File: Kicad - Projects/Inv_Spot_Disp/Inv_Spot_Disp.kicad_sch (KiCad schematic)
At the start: 38 parts, among them J1 PWM_Out, J2 Power_Supply, J3 Trigger, J4 Prog, SW1 1, SW2 2, SW3 3, SW4 4, SW5 SW_Push, U1 STM32F030F4Px, U2 NHD-0420H1Z, U3 AMS1117-3.3, U4 LKS561, U5 L7805, U6 LTV-817S

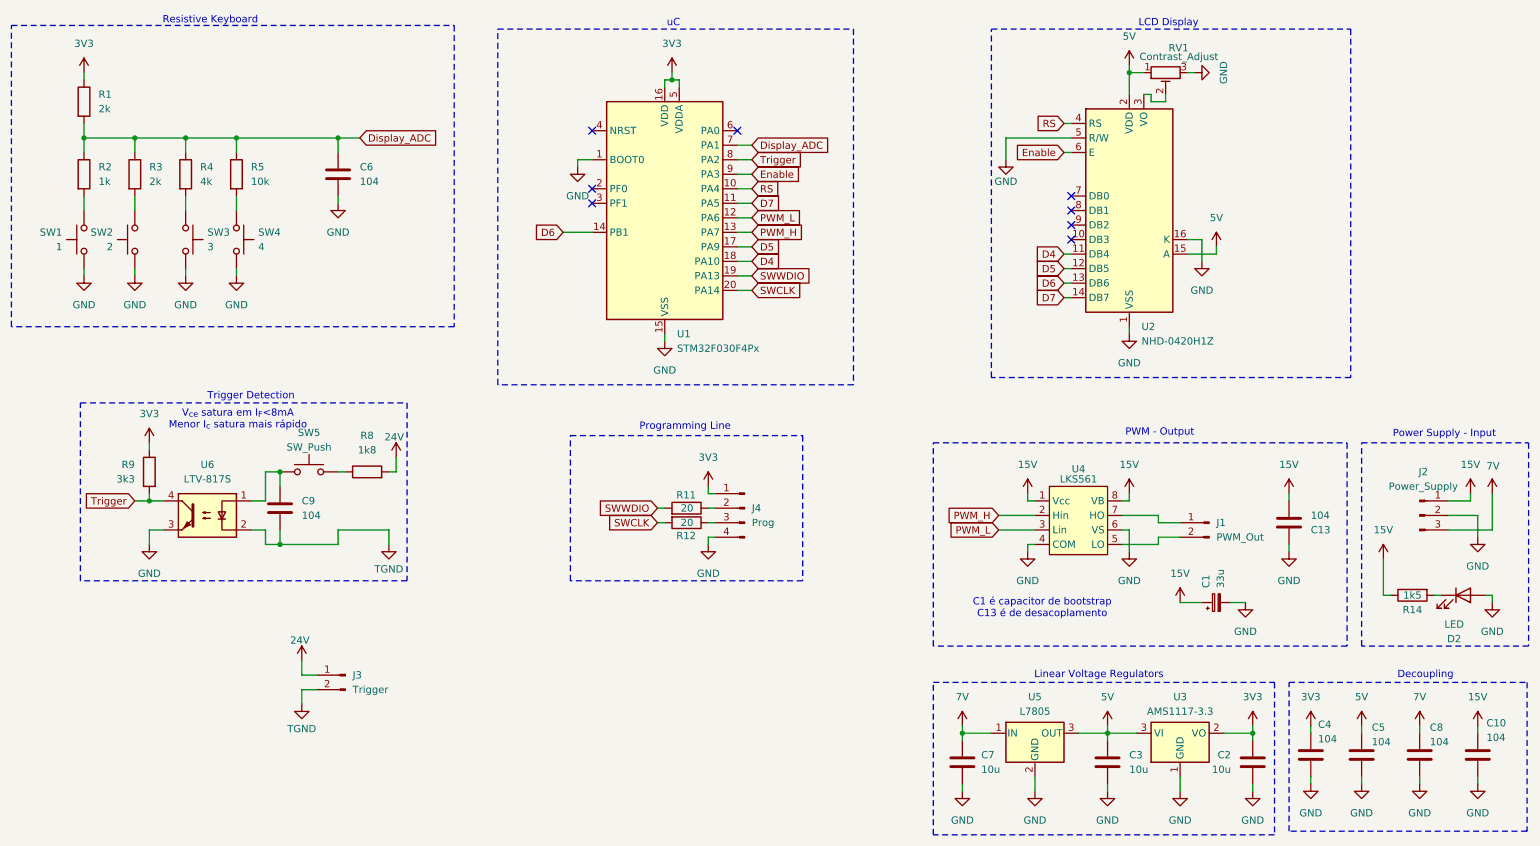
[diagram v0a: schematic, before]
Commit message: Adicionada Fuaração
Adicionada furação de montagem na placa de display, 4 furos M3 nos cantos da placa
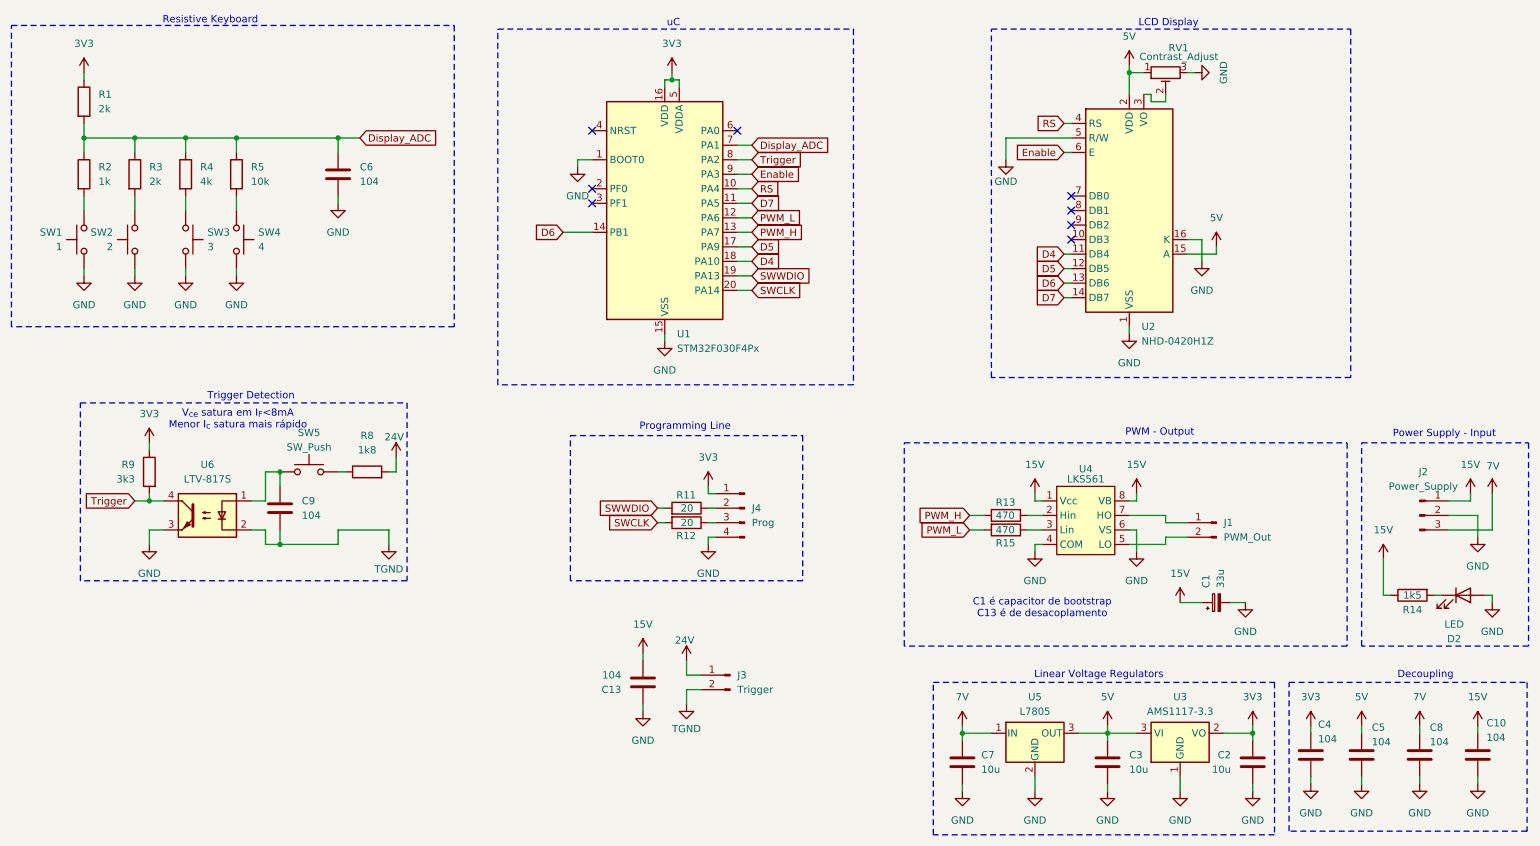
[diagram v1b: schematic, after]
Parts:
- added R13, R15: 470, Resistor_SMD:R_0805_2012Metric, symbol Device:R
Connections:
- net PWM_H: now also R13.2; no longer U4.2 (Hin)
- net PWM_L: now also R15.2; no longer U4.3 (Lin)
- new net: R13.1, U4.2 (Hin)
- new net: R15.1, U4.3 (Lin)
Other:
- moved on the sheet: C13, J1, J3, U4

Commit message: Finalização da Nova Placa de Potência
Dissipadores reorientados e reposicionados para melhor fluxo de ar

Ajuste dos footprints para dissipadores

Adição de resistores na placa de display para melhor proteção do STM32 e redução do brilho da LCD
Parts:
- removed C6: 104, Capacitor_SMD:C_1206_3216Metric_Pad1.33x1.80mm_HandSolder, symbol Device:C
- added R16: 100, Resistor_SMD:R_1206_3216Metric, symbol Device:R
- R1: value 2k -> 2k2
- R13, R15: value 470 -> 100; footprint Resistor_SMD:R_0805_2012Metric -> Resistor_SMD:R_1206_3216Metric
- R2: value 1k -> 10k
- R3: value 2k -> 4k7
- R4: value 4k -> 2k2
- R5: value 10k -> 1k
- R8: value 1k8 -> 2k2
- R9: value 3k3 -> 4k7
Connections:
- net 5V: now also R16.1; no longer U2.15 (A)
- new net: R16.2, U2.15 (A)
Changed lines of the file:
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@@
 	)
 	(junction
-		(at 73.66 39.37)
-		(diameter 0)
-		(color 0 0 0 0)
-	)
-	(junction
 		(at 29.21 39.37)
 		(diameter 0)
@@
 	)
 	(junction
-		(at 55.88 39.37)
+		(at 40.64 102.87)
 		(diameter 0)
 		(color 0 0 0 0)
@@
 	)
 	(junction
-		(at 40.64 102.87)
+		(at 46.99 39.37)
 		(diameter 0)
 		(color 0 0 0 0)
 	)
 	(junction
-		(at 46.99 39.37)
+		(at 132.08 29.21)
 		(diameter 0)
 		(color 0 0 0 0)
 	)
 	(junction
-		(at 132.08 29.21)
+		(at 38.1 39.37)
 		(diameter 0)
 		(color 0 0 0 0)
 	)
 	(junction
-		(at 38.1 39.37)
+		(at 55.88 39.37)
 		(diameter 0)
 		(color 0 0 0 0)
@@
 	(wire
 		(pts
+			(xy 233.68 59.69) (xy 234.95 59.69)
+		)
+		(stroke
+			(width 0)
+			(type default)
+		)
+	)
+	(wire
+		(pts
 			(xy 223.52 27.94) (xy 222.25 27.94)
 		)
@@
 	(wire
 		(pts
-			(xy 73.66 39.37) (xy 73.66 41.91)
+			(xy 196.85 110.49) (xy 195.58 110.49)
 		)
 		(stroke
@@
 	(wire
 		(pts
-			(xy 196.85 110.49) (xy 195.58 110.49)
+			(xy 267.97 107.95) (xy 275.59 107.95)
 		)
 		(stroke
@@
 	(wire
 		(pts
-			(xy 267.97 107.95) (xy 275.59 107.95)
+			(xy 222.25 59.69) (xy 226.06 59.69)
 		)
 		(stroke
@@
 	(wire
 		(pts
-			(xy 73.66 49.53) (xy 73.66 50.8)
-		)
-		(stroke
-			(width 0)
-			(type default)
-		)
-	)
-	(wire
-		(pts
 			(xy 82.55 110.49) (xy 82.55 107.95)
 		)
@@
 	(wire
 		(pts
-			(xy 222.25 59.69) (xy 227.33 59.69)
-		)
-		(stroke
-			(width 0)
-			(type default)
-		)
-	)
-	(wire
-		(pts
 			(xy 115.57 44.45) (xy 115.57 43.18)
 		)
@@
 	(wire
 		(pts
-			(xy 227.33 59.69) (xy 227.33 58.42)
+			(xy 234.95 59.69) (xy 234.95 57.15)
 		)
 		(stroke
@@
 	(wire
 		(pts
-			(xy 77.47 39.37) (xy 73.66 39.37)
-		)
-		(stroke
-			(width 0)
-			(type default)
-		)
-	)
-	(wire
-		(pts
 			(xy 203.2 143.51) (xy 208.28 143.51)
 		)
@@
 	(wire
 		(pts
-			(xy 55.88 39.37) (xy 73.66 39.37)
+			(xy 55.88 39.37) (xy 66.04 39.37)
 		)
 		(stroke
@@
 	(global_label "Display_ADC"
 		(shape input)
-		(at 77.47 39.37 0)
+		(at 66.04 39.37 0)
 		(fields_autoplaced yes)
 		(effects
@@
 		)
 		(property "Intersheetrefs" "${INTERSHEET_REFS}"
-			(at 91.8851 39.37 0)
+			(at 80.4551 39.37 0)
 			(hide yes)
 			(show_name no)
@@
 			)
 		)
-		(property "Value" "3k3"
+		(property "Value" "4k7"
 			(at 38.1 99.0599 0)
 			(show_name no)
@@
 			)
 		)
-		(property "Value" "1k8"
+		(property "Value" "2k2"
 			(at 78.74 93.98 90)
 			(show_name no)
@@
 	(symbol
 		(lib_id "power:VCC")
-		(at 227.33 58.42 0)
+		(at 234.95 57.15 0)
 		(unit 1)
 		(body_style 1)
@@
 		(fields_autoplaced yes)
 		(property "Reference" "#PWR015"
-			(at 227.33 62.23 0)
+			(at 234.95 60.96 0)
 			(hide yes)
 			(show_name no)
@@
 		)
 		(property "Value" "5V"
-			(at 227.33 53.34 0)
+			(at 234.95 52.07 0)
 			(show_name no)
 			(do_not_autoplace no)
@@
 		)
 		(property "Footprint" ""
-			(at 227.33 58.42 0)
+			(at 234.95 57.15 0)
 			(hide yes)
 			(show_name no)
@@
 		)
 		(property "Datasheet" ""
-			(at 227.33 58.42 0)
+			(at 234.95 57.15 0)
 			(hide yes)
 			(show_name no)
@@
 		)
 		(property "Description" "Power symbol creates a global label with name \"VCC\""
-			(at 227.33 58.42 0)
+			(at 234.95 57.15 0)
 			(hide yes)
 			(show_name no)
@@
 			)
 		)
-		(property "Value" "10k"
+		(property "Value" "1k"
 			(at 58.42 46.9899 0)
 			(show_name no)
@@
 	(symbol
 		(lib_id "power:GND")
-		(at 73.66 50.8 0)
+		(at 127 139.7 0)
+		(mirror y)
 		(unit 1)
 		(body_style 1)
@@
 		(dnp no)
 		(fields_autoplaced yes)
-		(property "Reference" "#PWR033"
-			(at 73.66 57.15 0)
+		(property "Reference" "#PWR050"
+			(at 127 146.05 0)
 			(hide yes)
 			(show_name no)
@@
 		)
 		(property "Value" "GND"
-			(at 73.66 55.88 0)
+			(at 127 144.78 0)
 			(show_name no)
 			(do_not_autoplace no)
@@
 		)
 		(property "Footprint" ""
-			(at 73.66 50.8 0)
+			(at 127 139.7 0)
 			(hide yes)
 			(show_name no)
@@
 		)
 		(property "Datasheet" ""
-			(at 73.66 50.8 0)
+			(at 127 139.7 0)
 			(hide yes)
 			(show_name no)
@@
 		)
 		(property "Description" "Power symbol creates a global label with name \"GND\" , ground"
-			(at 73.66 50.8 0)
+			(at 127 139.7 0)
 			(hide yes)
 			(show_name no)
@@
 			(project "Inv_Spot_Disp"
 				(path "/016976b8-e488-405d-b5a2-1b3e7431e7ce"
-					(reference "#PWR033")
+					(reference "#PWR050")
 					(unit 1)
 				)
@@
 	)
 	(symbol
-		(lib_id "power:GND")
-		(at 127 139.7 0)
-		(mirror y)
+		(lib_id "Device:R")
+		(at 229.87 59.69 270)
+		(mirror x)
 		(unit 1)
 		(body_style 1)
@@
 		(in_pos_files yes)
 		(dnp no)
-		(fields_autoplaced yes)
-		(property "Reference" "#PWR050"
-			(at 127 146.05 0)
-			(hide yes)
+		(property "Reference" "R16"
+			(at 228.092 57.404 90)
 			(show_name no)
 			(do_not_autoplace no)
@@
 					(size 1.27 1.27)
 				)
+				(justify left)
 			)
 		)
-		(property "Value" "GND"
-			(at 127 144.78 0)
+		(property "Value" "100"
+			(at 228.092 59.69 90)
 			(show_name no)
 			(do_not_autoplace no)
@@
 					(size 1.27 1.27)
 				)
+				(justify left)
 			)
 		)
-		(property "Footprint" ""
-			(at 127 139.7 0)
+		(property "Footprint" "Resistor_SMD:R_1206_3216Metric"
+			(at 229.87 61.468 90)
 			(hide yes)
 			(show_name no)
@@
 		)
 		(property "Datasheet" ""
-			(at 127 139.7 0)
+			(at 229.87 59.69 0)
 			(hide yes)
 			(show_name no)
@@
 			)
 		)
-		(property "Description" "Power symbol creates a global label with name \"GND\" , ground"
-			(at 127 139.7 0)
+		(property "Description" "Resistor"
+			(at 229.87 59.69 0)
 			(hide yes)
 			(show_name no)
@@
 			)
 		)
+		(pin "2"
+		)
 		(pin "1"
 		)
@@
 			(project "Inv_Spot_Disp"
 				(path "/016976b8-e488-405d-b5a2-1b3e7431e7ce"
-					(reference "#PWR050")
+					(reference "R16")
 					(unit 1)
 				)
@@
 			)
 		)
-		(property "Value" "470"
+		(property "Value" "100"
 			(at 188.722 105.41 90)
 			(show_name no)
@@
 			)
 		)
-		(property "Footprint" "Resistor_SMD:R_0805_2012Metric"
+		(property "Footprint" "Resistor_SMD:R_1206_3216Metric"
 			(at 190.5 107.188 90)
 			(hide yes)
@@
 			)
 		)
-		(property "Value" "2k"
+		(property "Value" "4k7"
 			(at 40.64 46.9899 0)
 			(show_name no)
@@
 			)
 		)
-		(property "Value" "470"
+		(property "Value" "100"
 			(at 188.722 107.95 90)
 			(show_name no)
@@
 			)
 		)
-		(property "Footprint" "Resistor_SMD:R_0805_2012Metric"
+		(property "Footprint" "Resistor_SMD:R_1206_3216Metric"
 			(at 190.5 106.172 90)
 			(hide yes)
@@
 			)
 		)
-		(property "Value" "1k"
+		(property "Value" "10k"
 			(at 31.75 46.9899 0)
 			(show_name no)
@@
 			)
 		)
-		(property "Value" "2k"
+		(property "Value" "2k2"
 			(at 31.75 34.2899 0)
 			(show_name no)
@@
 	)
 	(symbol
-		(lib_id "Device:C")
-		(at 73.66 45.72 0)
-		(unit 1)
-		(body_style 1)
-		(exclude_from_sim no)
-		(in_bom yes)
-		(on_board yes)
-		(in_pos_files yes)
-		(dnp no)
-		(fields_autoplaced yes)
-		(property "Reference" "C6"
-			(at 77.47 44.4499 0)
-			(show_name no)
-			(do_not_autoplace no)
-			(effects
-				(font
-					(size 1.27 1.27)
-				)
-				(justify left)
-			)
-		)
-		(property "Value" "104"
-			(at 77.47 46.9899 0)
-			(show_name no)
-			(do_not_autoplace no)
-			(effects
-				(font
-					(size 1.27 1.27)
-				)
-				(justify left)
-			)
-		)
-		(property "Footprint" "Capacitor_SMD:C_1206_3216Metric_Pad1.33x1.80mm_HandSolder"
-			(at 74.6252 49.53 0)
-			(hide yes)
-			(show_name no)
-			(do_not_autoplace no)
-			(effects
-				(font
-					(size 1.27 1.27)
-				)
-			)
-		)
-		(property "Datasheet" ""
-			(at 73.66 45.72 0)
-			(hide yes)
-			(show_name no)
-			(do_not_autoplace no)
-			(effects
-				(font
-					(size 1.27 1.27)
-				)
-			)
-		)
-		(property "Description" "Unpolarized capacitor"
-			(at 73.66 45.72 0)
-			(hide yes)
-			(show_name no)
-			(do_not_autoplace no)
-			(effects
-				(font
-					(size 1.27 1.27)
-				)
-			)
-		)
-		(pin "1"
-		)
-		(pin "2"
-		)
-		(instances
-			(project "Inv_Spot_Disp"
-				(path "/016976b8-e488-405d-b5a2-1b3e7431e7ce"
-					(reference "C6")
-					(unit 1)
-				)
-			)
-		)
-	)
-	(symbol
 		(lib_id "power:VCC")
 		(at 220.98 120.65 0)
@@
 			)
 		)
-		(property "Value" "4k"
+		(property "Value" "2k2"
 			(at 49.53 46.9899 0)
 			(show_name no)

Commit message: Preparação para Manufatura
Validação de footprints

Serigrafia movida para melhorar legibilidade

Backup de versão com trafo anterior salvo

Adição de snippet de código para ativação da proteção térmica
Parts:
- added R10: 4k7, Resistor_SMD:R_1206_3216Metric_Pad1.30x1.75mm_HandSolder, symbol Device:R
- added R17: 2k2, Resistor_SMD:R_1206_3216Metric_Pad1.30x1.75mm_HandSolder, symbol Device:R
- added U7: LTV-817S, Package_DIP:SMDIP-4_W9.53mm, symbol Isolator:LTV-817S
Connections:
- net 15V: now also R17.2
- net 3V3: now also R10.1
- net GND: now also U7.2, U7.3
- net Temp_Sig: now reaches U1.3 (PF1)
- net Temp_Sig: now also R10.2, U7.4
- new net: R17.1, U7.1
- no-connect marks 8 -> 7
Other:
- note added: "Safety Detection"

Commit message: Finalização - Placa Protótipo
Versão final da placa protótipo - placa já validada

Alterações:
 - Melhoras no plano terra para retorno de potência
 - Blindagem das trilhas de PWM para os IGBTs inferiores
 - Alargamento das trilhas de saída para a retificação

Falta:
 - Colocar todos os SMDs no lado TOP da placa
 - Ajustar posição dos IGBTs e transformador
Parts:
- C1: value 33u -> 100u
- C2, C3, C7: footprint Capacitor_THT:C_Radial_D10.0mm_H12.5mm_P5.00mm -> Capacitor_THT:CP_Radial_D10.0mm_P5.00mm
- R14: value 1k5 -> 2k2
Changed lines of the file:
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@@
 			)
 		)
-		(property "Footprint" "Capacitor_THT:C_Radial_D10.0mm_H12.5mm_P5.00mm"
+		(property "Footprint" "Capacitor_THT:CP_Radial_D10.0mm_P5.00mm"
 			(at 183.8452 152.4 0)
 			(hide yes)
@@
 		(fields_autoplaced yes)
 		(property "Reference" "C1"
-			(at 225.5138 118.11 0)
+			(at 226.7839 114.3 90)
 			(show_name no)
 			(do_not_autoplace no)
@@
 					(size 1.27 1.27)
 				)
-				(justify left)
 			)
 		)
-		(property "Value" "33u"
-			(at 228.0538 118.11 0)
+		(property "Value" "100u"
+			(at 226.7839 116.84 90)
 			(show_name no)
 			(do_not_autoplace no)
@@
 					(size 1.27 1.27)
 				)
-				(justify left)
 			)
 		)
@@
 			)
 		)
-		(property "Value" "1k5"
+		(property "Value" "2k2"
 			(at 261.62 119.38 90)
 			(show_name no)
@@
 			)
 		)
-		(property "Footprint" "Capacitor_THT:C_Radial_D10.0mm_H12.5mm_P5.00mm"
+		(property "Footprint" "Capacitor_THT:CP_Radial_D10.0mm_P5.00mm"
 			(at 232.7148 152.4 0)
 			(hide yes)
@@
 			)
 		)
-		(property "Footprint" "Capacitor_THT:C_Radial_D10.0mm_H12.5mm_P5.00mm"
+		(property "Footprint" "Capacitor_THT:CP_Radial_D10.0mm_P5.00mm"
 			(at 209.2452 152.4 0)
 			(hide yes)
